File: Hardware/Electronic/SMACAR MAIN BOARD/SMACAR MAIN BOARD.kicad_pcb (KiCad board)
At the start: 2 copper layers, 9 parts, among them J2 USB_C_Receptacle_USB2.0_14P, U2 ESP32-S3-DevKitC

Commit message: Placa Terminada y Revisada por Camila Fernandez
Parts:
- removed R1, R2: 5.6k, Resistor_THT:R_Axial_DIN0207_L6.3mm_D2.5mm_P10.16mm_Horizontal
- added R1_5.6k1: 470R_0805_350mW, PCM_4ms_Resistor:R_0805_2012Metric, F.Cu at (147.8, 50.5)
- added R2_5.6k1: 470R_0805_350mW, PCM_4ms_Resistor:R_0805_2012Metric, F.Cu at (147.8, 54.5)
- added R3_10k1: 470R_0805_350mW, PCM_4ms_Resistor:R_0805_2012Metric, F.Cu at (114.8, 70.1)
- added R4_10k1: 470R_0805_350mW, PCM_4ms_Resistor:R_0805_2012Metric, F.Cu at (114.5, 56.5)
- added REF**: MountingHole_2.2mm_M2_DIN965_Pad, MountingHole:MountingHole_2.2mm_M2_DIN965_Pad, F.Cu at (106.0, 98.2)
- added REF**: MountingHole_2.2mm_M2_DIN965_Pad, MountingHole:MountingHole_2.2mm_M2_DIN965_Pad, F.Cu at (106.0, 25.5)
- added REF**: MountingHole_2.2mm_M2_DIN965_Pad, MountingHole:MountingHole_2.2mm_M2_DIN965_Pad, F.Cu at (157.2, 98.2)
- added REF**: MountingHole_2.2mm_M2_DIN965_Pad, MountingHole:MountingHole_2.2mm_M2_DIN965_Pad, F.Cu at (156.8, 25.5)
- MOLEX1: value M03PTH -> E-C SENSOR
- MOLEX2: value M03PTH -> PH
- MOLEX3: value M03PTH -> TDS SENSOR
- MOLEX4: value M03PTH -> TEMP
- MOLEX5: value M04PTH -> LORAWAN
- moved J2 31.1 mm to (156.5, 57.0), turned to 90 degrees
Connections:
- J2 pad A4: Net-(J2-VBUS-PadA4) -> 5V
- J2 pad A9: Net-(J2-VBUS-PadA4) -> 5V
- J2 pad B4: Net-(J2-VBUS-PadA4) -> 5V
- J2 pad B9: Net-(J2-VBUS-PadA4) -> 5V
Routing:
- net 5V: track 0.00 -> 143.3 mm
- net GND: track 42.3 -> 151.2 mm
- net Net-(R3_10k1-Pad2): track 0.00 -> 39.7 mm, vias 0 -> 1
- net SDA: track 0.00 -> 26.4 mm
- net SCL: track 0.00 -> 23.8 mm
- net Net-(J2-CC1): track 0.00 -> 13.5 mm
- net TEMP SENSOR: track 57.5 -> 63.7 mm, vias 0 -> 1
- net Net-(J2-CC2): track 0.00 -> 5.40 mm
- added copper zone on B.Cu, net GND
- added copper zone on F.Cu, net GND
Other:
- board text added: "MAIN BOARD SMACAR"

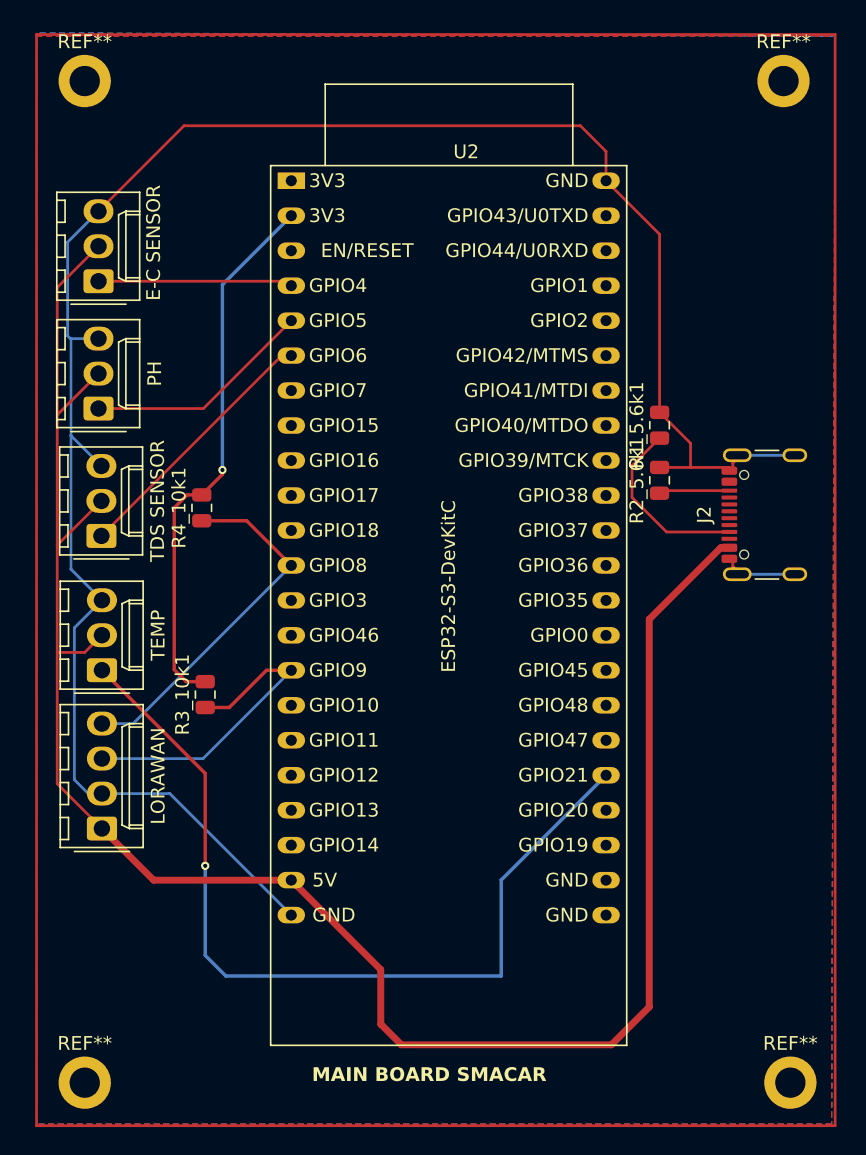
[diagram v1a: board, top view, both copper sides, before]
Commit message: Arreglo de Antena del esp32
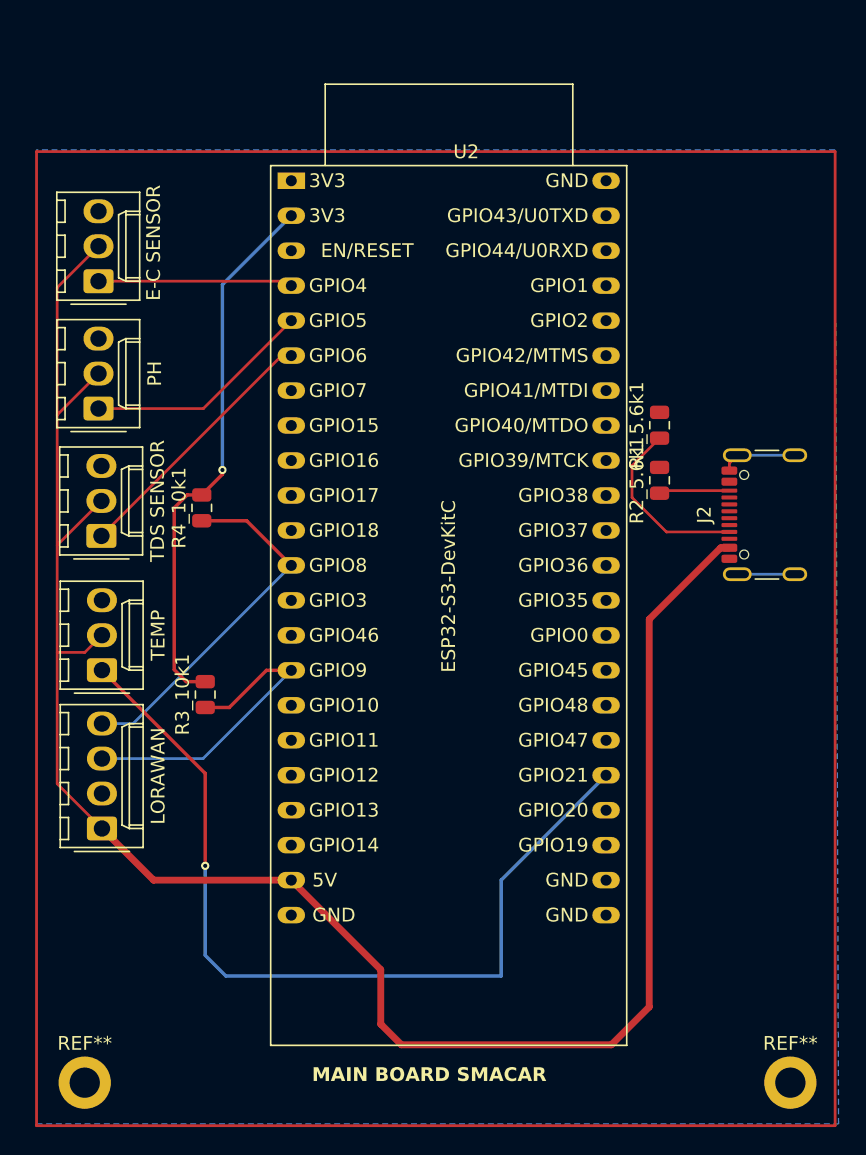
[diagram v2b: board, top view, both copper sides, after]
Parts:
- removed the REF** at (106.0, 25.5)
- removed the REF** at (156.8, 25.5)
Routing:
- net GND: track 151.2 -> 11.1 mm
